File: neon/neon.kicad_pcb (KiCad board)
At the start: 2 copper layers, 52.7 x 49.5 mm, 45 parts, among them J2 V3V3-GND, J3 V3V3-GND, J4 V3V3-GND, J5 V3V3-VIO, Q1 BC807, Q2 BC807, Q3 BC807, Q4 BC807, Q5 BC807, Q6 BC807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

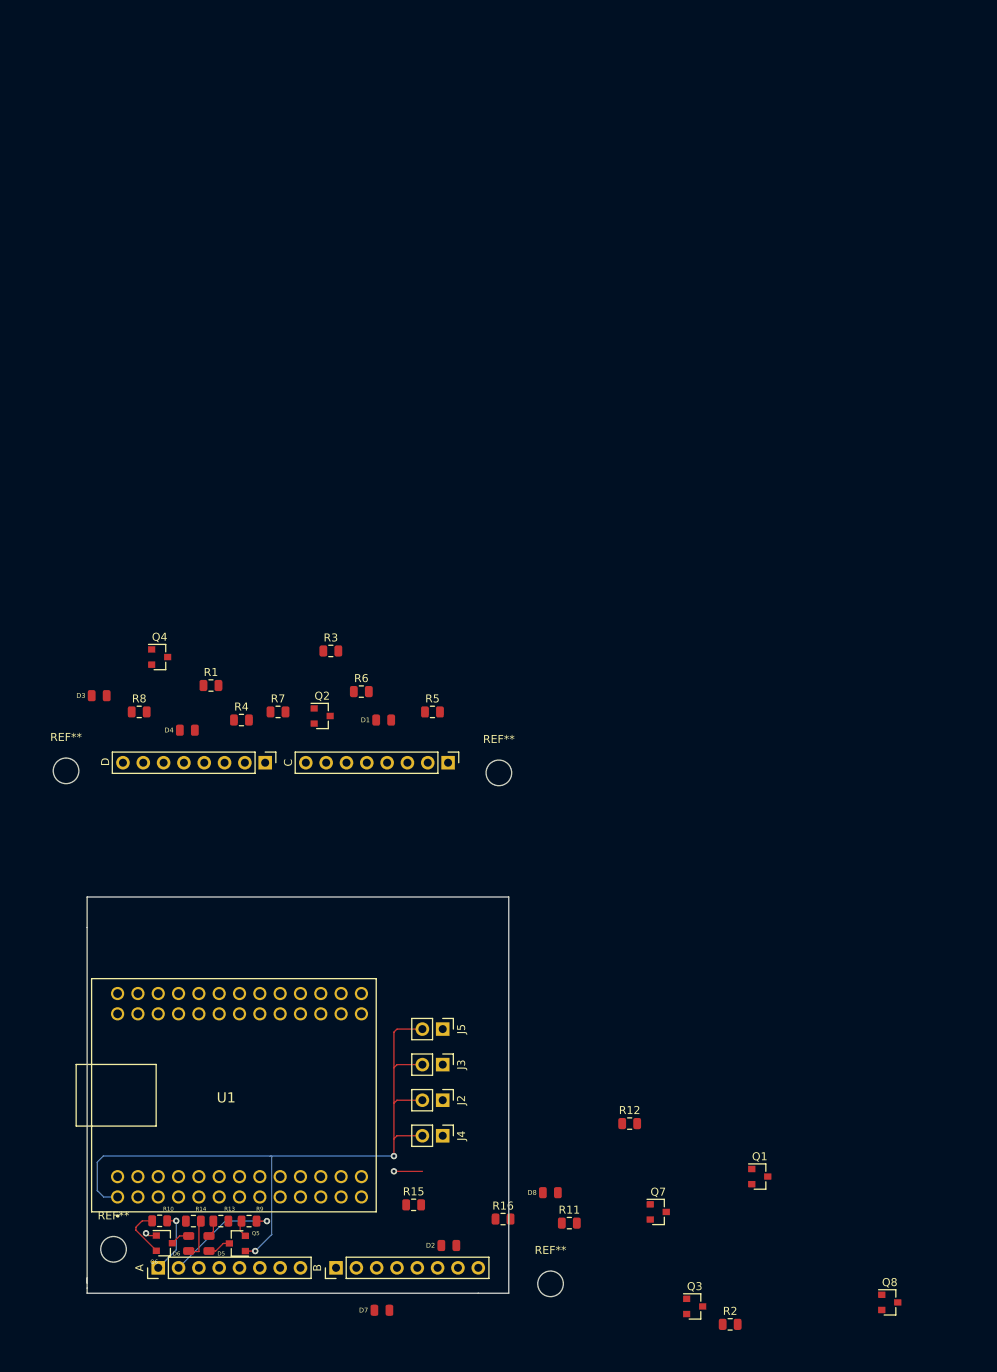
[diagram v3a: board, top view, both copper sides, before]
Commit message: FTDI centered (almost)
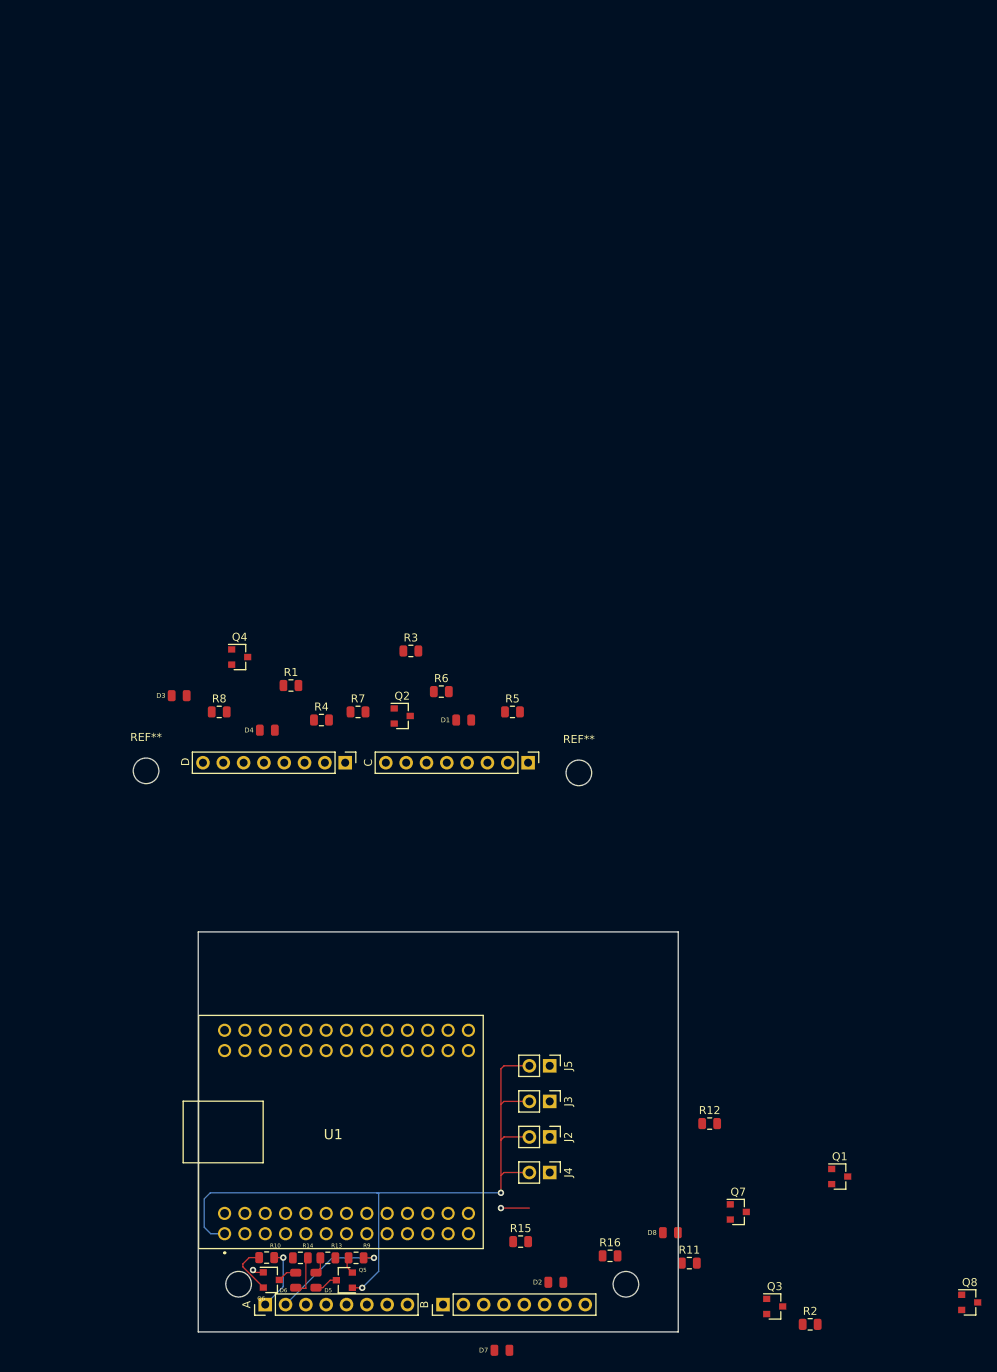
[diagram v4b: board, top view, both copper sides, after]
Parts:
- removed the REF** at (159.5, 123.9)
- removed the REF** at (153.1, 60.0)
- removed the REF** at (99.0, 59.8)
- added REF**: MountingHole_3.2mm_M3, MountingHole:MountingHole_3.2mm_M3, F.Cu at (168.9, 124.0)
- added REF**: MountingHole_3.2mm_M3, MountingHole:MountingHole_3.2mm_M3, F.Cu at (163.1, 60.0)
- added REF**: MountingHole_3.2mm_M3, MountingHole:MountingHole_3.2mm_M3, F.Cu at (109.0, 59.8)
- moved REF** 16.2 mm to (120.5, 124.0)
- moved D7 15.8 mm to (153.4, 132.2)
- moved D8 15.8 mm to (174.5, 117.5)
- moved R11 15.8 mm to (176.9, 121.3)
- moved A 14.1 mm to (123.9, 126.5)
- moved B 14.1 mm to (146.1, 126.5)
- moved D5 14.1 mm to (130.2, 123.5)
- moved D6 14.1 mm to (127.7, 123.5)
- moved Q5 14.1 mm to (133.8, 123.5)
- moved Q6 14.1 mm to (124.6, 123.4)
- moved R10 14.1 mm to (124.0, 120.6)
- moved R16 14.1 mm to (167.0, 120.4)
- moved R9 14.1 mm to (135.2, 120.7)
- moved R13 14.1 mm to (131.7, 120.7)
- moved R14 14.1 mm to (128.3, 120.7)
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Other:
- board size 52.7 x 49.5 mm -> 60 x 50 mm

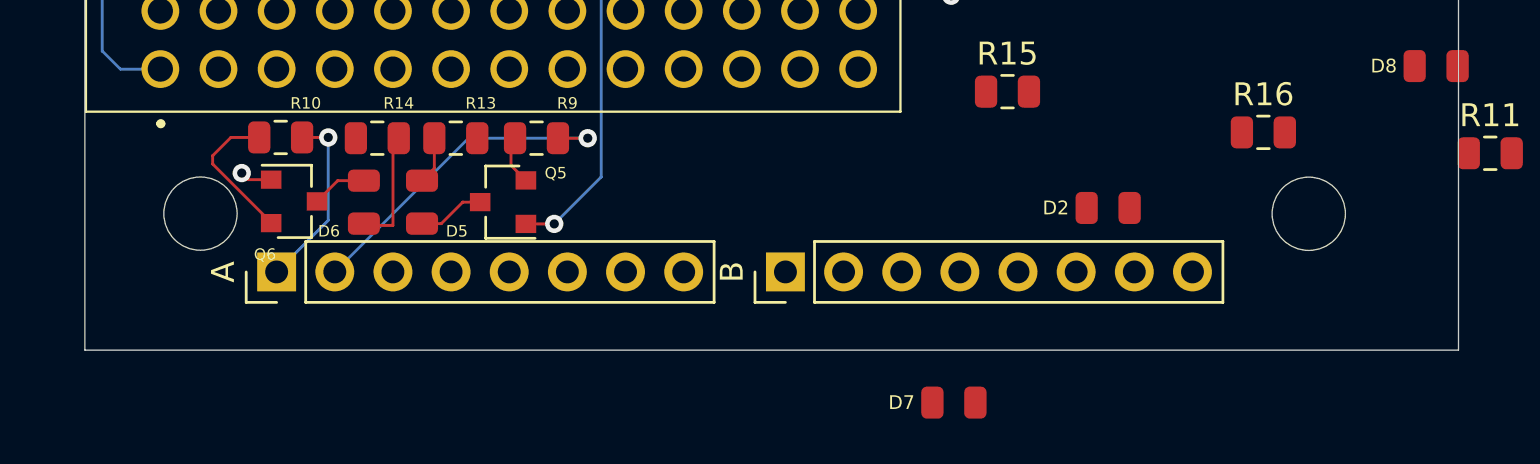
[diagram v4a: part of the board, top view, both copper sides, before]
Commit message: Restore lost pin
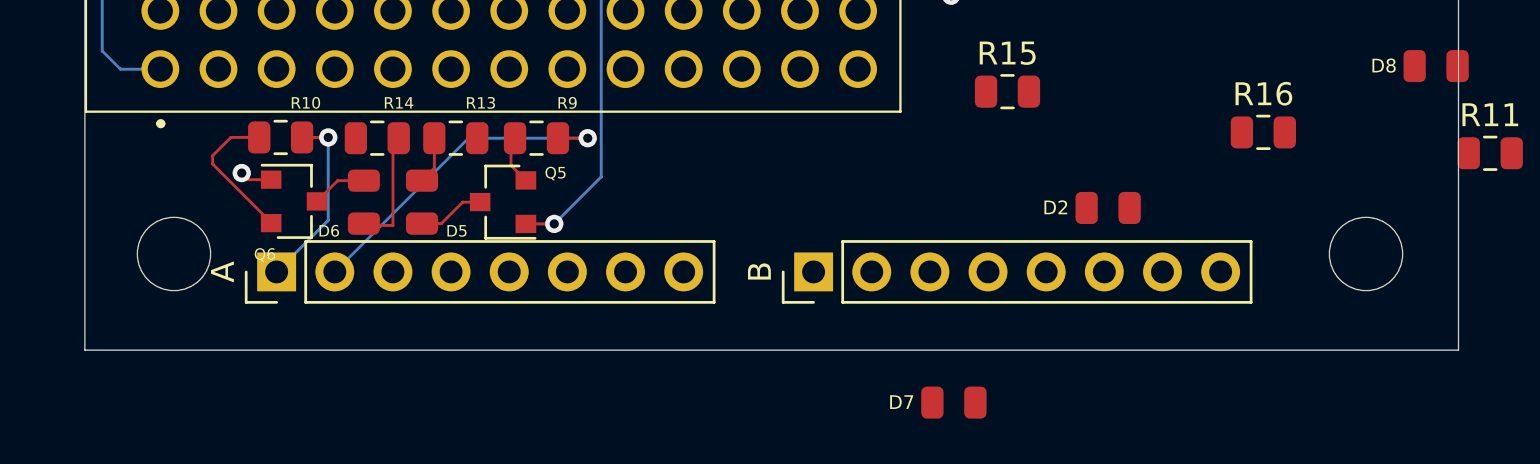
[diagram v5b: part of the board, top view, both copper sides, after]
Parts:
- moved REF** 3.06 mm to (171.4, 125.7)
- moved REF** 2.11 mm to (119.4, 125.7)
- moved B 1.23 mm to (147.3, 126.5)
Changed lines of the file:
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@@
   )
   (module MountingHole:MountingHole_3.2mm_M3 (layer F.Cu)
-    (at 168.9494 123.9736)
+    (at 171.45 125.73)
     (descr "Mounting Hole 3.2mm, no annular, M3")
     (tags "mounting hole 3.2mm no annular m3")
@@
   )
   (module MountingHole:MountingHole_3.2mm_M3 (layer F.Cu)
-    (at 120.537 123.967)
+    (at 119.38 125.73)
     (descr "Mounting Hole 3.2mm, no annular, M3")
     (tags "mounting hole 3.2mm no annular m3")
@@
   )
   (module Connector_PinHeader_2.54mm:PinHeader_1x08_P2.54mm_Vertical (layer F.Cu)
-    (at 146.0894 126.5136 90)
+    (at 147.32 126.5136 90)
     (descr "Through hole straight pin header, 1x08, 2.54mm pitch, single row")
     (tags "Through hole pin header THT 1x08 2.54mm single row")
